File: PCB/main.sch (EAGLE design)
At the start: 52 parts, among them X1 BU-SMA-V

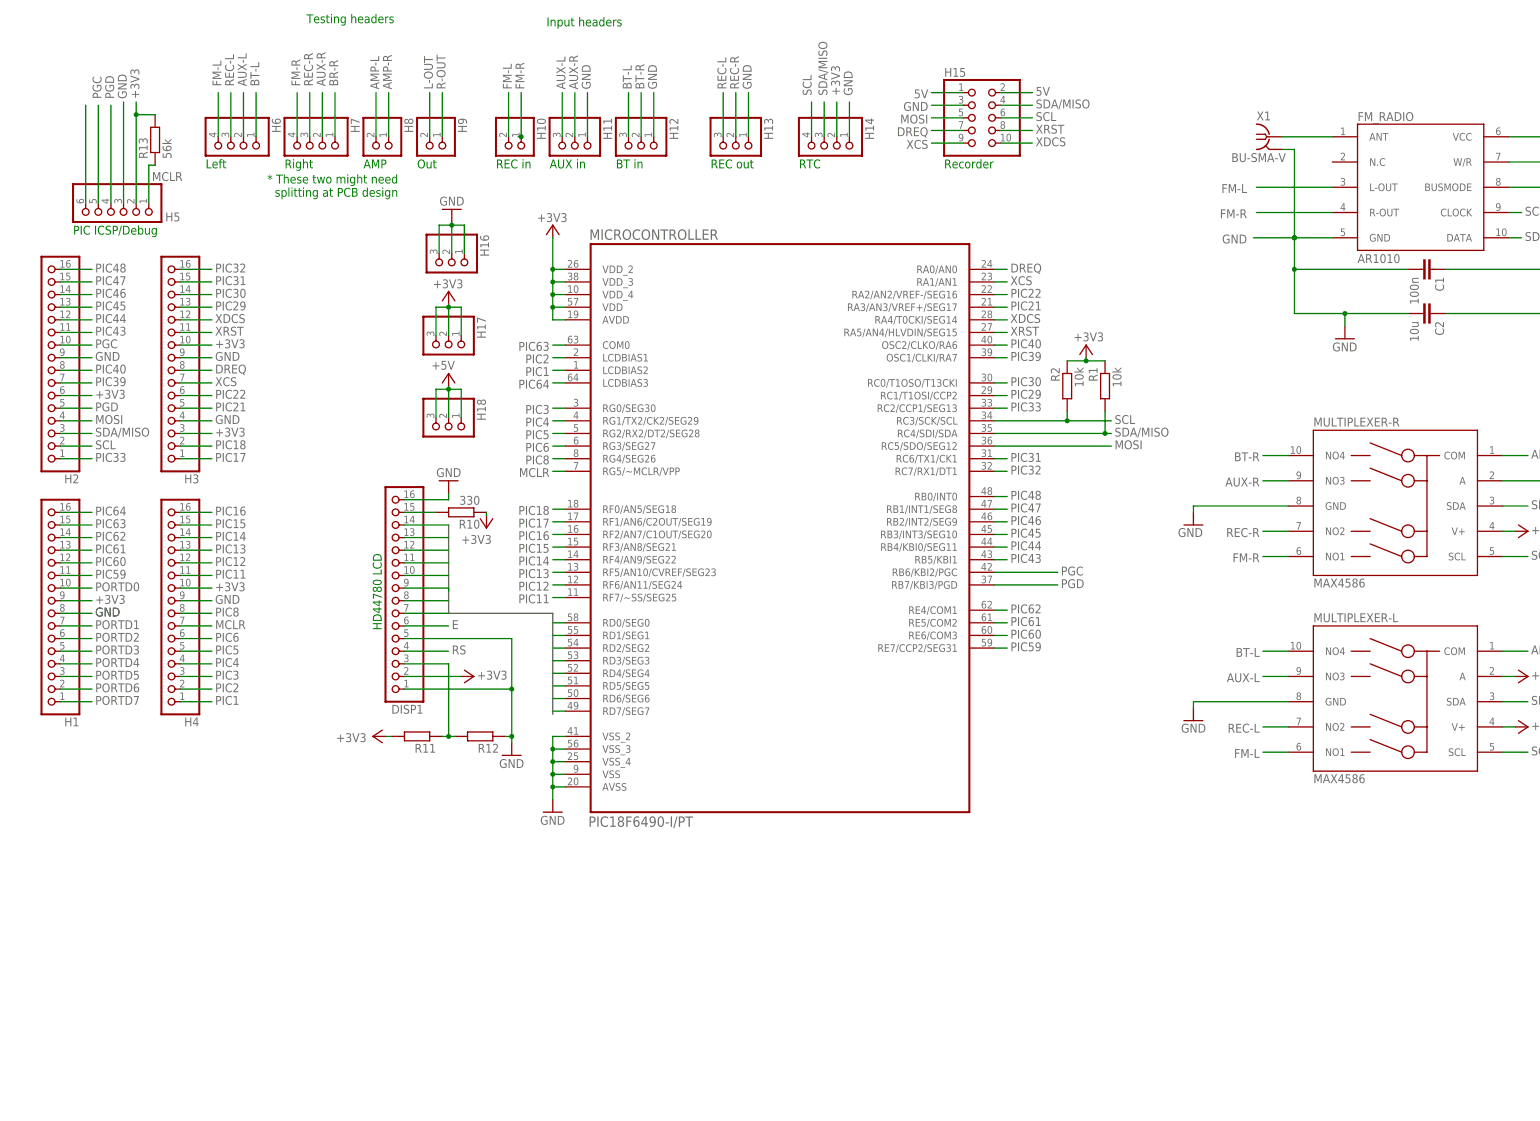
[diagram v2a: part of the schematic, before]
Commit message: Eagle Schematic Changes
Added level shifters
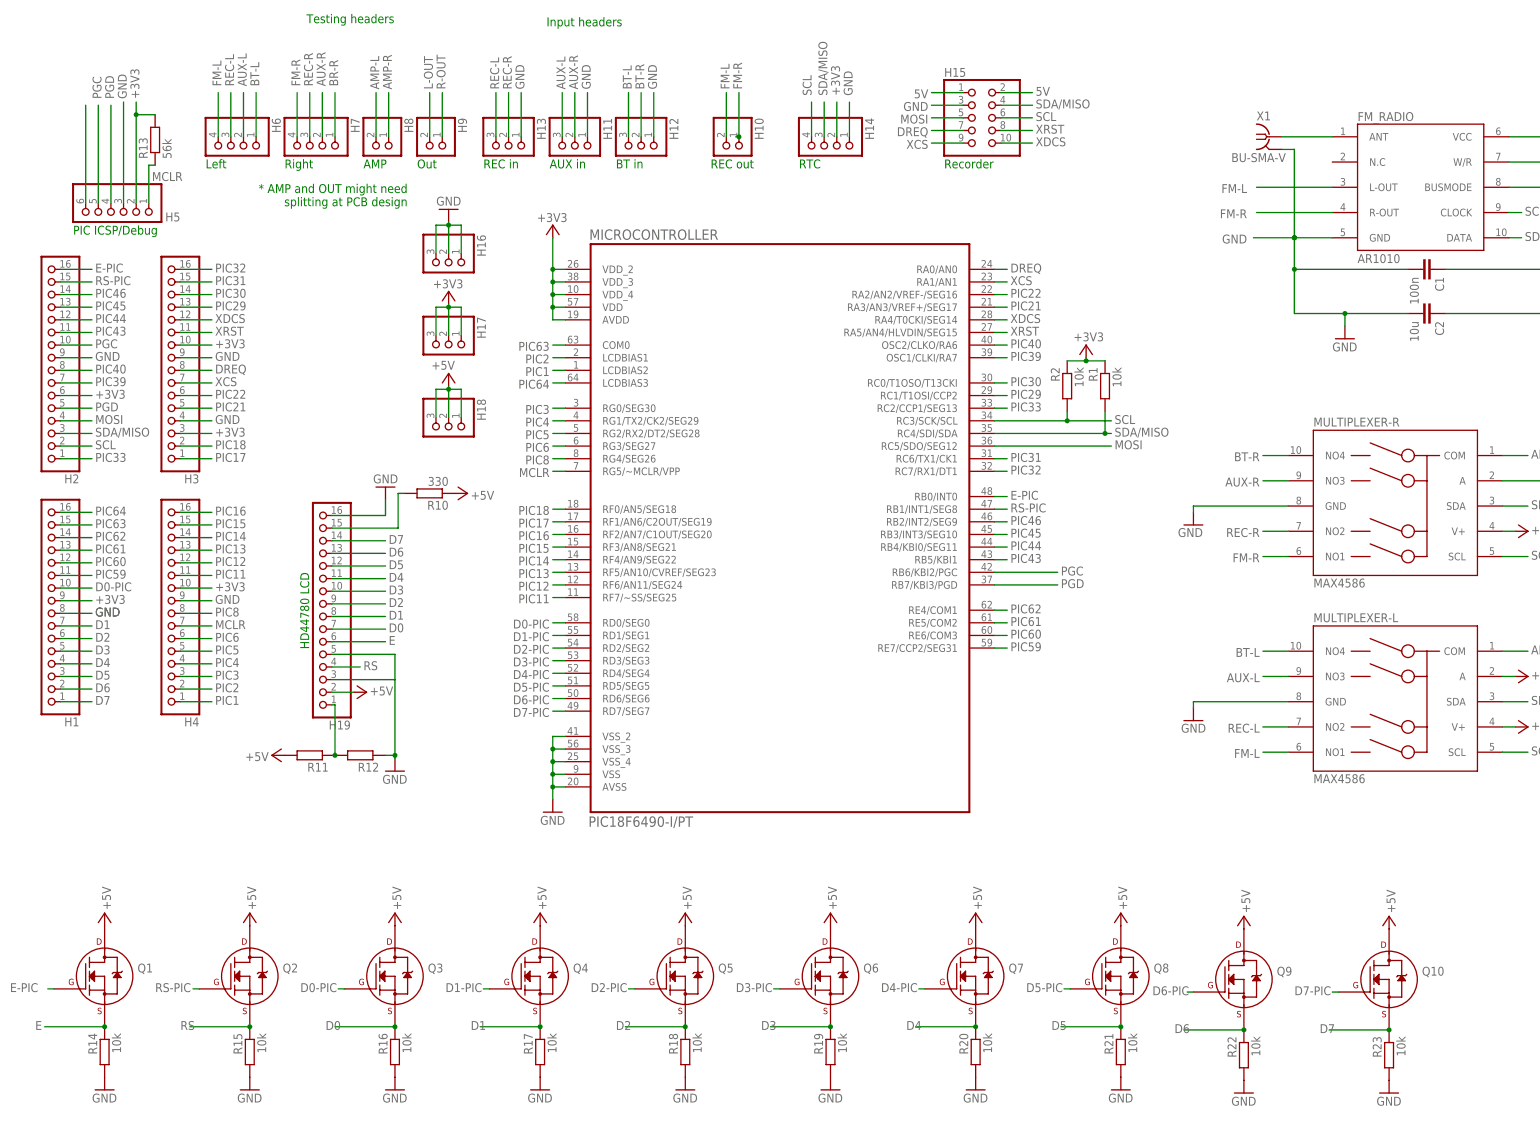
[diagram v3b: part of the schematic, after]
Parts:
- removed DISP1: (no value), pinhead:PINHD-1X16
- added H19: (no value), pinhead:PINHD-1X16
- added Q1, Q10, Q2, Q3, Q4, Q5, Q6, Q7, Q8, Q9: (no value), transistors:2N7000_SOT23
- added R14, R15, R16, R17, R18, R19, R20, R21, R22, R23: 10k, resistor:R-EU_M0805
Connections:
- removed net N$2: DISP1.15, R10.2
- removed net PIC47: H2.15, MICROCONTROLLER.RB1/INT1/SEG8
- removed net PIC48: H2.16, MICROCONTROLLER.RB0/INT0
- removed net PORTD0: DISP1.7, H1.10, MICROCONTROLLER.RD0/SEG0
- removed net PORTD1: DISP1.8, H1.7, MICROCONTROLLER.RD1/SEG1
- removed net PORTD2: DISP1.9, H1.6, MICROCONTROLLER.RD2/SEG2
- removed net PORTD3: DISP1.10, H1.5, MICROCONTROLLER.RD3/SEG3
- removed net PORTD4: DISP1.11, H1.4, MICROCONTROLLER.RD4/SEG4
- removed net PORTD5: DISP1.12, H1.3, MICROCONTROLLER.RD5/SEG5
- removed net PORTD6: DISP1.13, H1.2, MICROCONTROLLER.RD6/SEG6
- removed net PORTD7: DISP1.14, H1.1, MICROCONTROLLER.RD7/SEG7
- new net D0: H19.7, Q3.S, R16.1
- new net D0-PIC: H1.10, MICROCONTROLLER.RD0/SEG0, Q3.G
- new net D1: H1.7, H19.8, Q4.S, R17.1
- new net D1-PIC: MICROCONTROLLER.RD1/SEG1, Q4.G
- new net D2: H1.6, H19.9, Q5.S, R18.1
- new net D2-PIC: MICROCONTROLLER.RD2/SEG2, Q5.G
- new net D3: H1.5, H19.10, Q6.S, R19.1
- new net D3-PIC: MICROCONTROLLER.RD3/SEG3, Q6.G
- new net D4: H1.4, H19.11, Q7.S, R20.1
- new net D4-PIC: MICROCONTROLLER.RD4/SEG4, Q7.G
- new net D5: H1.3, H19.12, Q8.S, R21.1
- new net D5-PIC: MICROCONTROLLER.RD5/SEG5, Q8.G
- new net D6: H1.2, H19.13, Q9.S, R22.1
- new net D6-PIC: MICROCONTROLLER.RD6/SEG6, Q9.G
- new net D7: H1.1, H19.14, Q10.S, R23.1
- new net D7-PIC: MICROCONTROLLER.RD7/SEG7, Q10.G
- new net E-PIC: H2.16, MICROCONTROLLER.RB0/INT0, Q1.G
- new net N$20: H19.15, R10.2
- new net RS-PIC: H2.15, MICROCONTROLLER.RB1/INT1/SEG8, Q2.G
- net +3V3: no longer DISP1.2, R10.1, R11.2
- net +5V: now also H19.2, Q1.D, Q10.D, Q2.D, Q3.D, Q4.D, Q5.D, Q6.D, Q7.D, Q8.D, Q9.D, R10.1, R11.2
- net E: now also H19.6, Q1.S, R14.1; no longer DISP1.6
- net GND: now also H19.16, H19.3, H19.5, R14.2, R15.2, R16.2, R17.2, R18.2, R19.2, R20.2, R21.2, R22.2, R23.2; no longer DISP1.1, DISP1.16, DISP1.5
- net N$13: now also H19.1; no longer DISP1.3
- net RS: now also H19.4, Q2.S, R15.1; no longer DISP1.4
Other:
- note added: "* AMP and OUT might need splitting at PCB design"
- note removed: "* These two might need splitting at PCB design"
- moved on the sheet: H10, H13, H16, R10, R11, R12

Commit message: Initial PCB layout
~75% complete.
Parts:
- removed C6, C9: 470u, rcl:C-EUC0805
- removed R9: 4.7, resistor:R-EU_M0805
- added +5V: LSP11, solpad:LSP11
- added C13, C14, C15, C16, C17, C18: 100n, rcl:C-EUC0805
- added C20, C21: 100u, cap-pan40:C-PR-SMD-SV-D
- added R24, R25, R26: 10, resistor:R-EU_M0805
- C5, C8: value 100u -> 470u; device rcl:C-EUC0805 -> cap-pan40:C-PR-SMD-SV-G
- H6, H7: device pinhead:PINHD-1X4/90 -> pinhead:PINHD-1X4
- R6: value 4.7 -> 10
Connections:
- removed net N$12: AMP-R.-IN, C5.1
- removed net N$16: C10.2, R9.2
- new net N$1: AMP-R.-IN, C20.+
- new net N$10: C10.2, R25.2, R26.2
- new net N$2: +5V.MP, C4.1, VOLTAGE_REGULATOR.VIN
- net +3V3: now also C13.2, C14.2, C15.2, C16.2, C17.2, C18.2
- net +5V: no longer C4.1, VOLTAGE_REGULATOR.VIN
- net D1: no longer H1.7
- net D1-PIC: now also H1.7
- net D2: no longer H1.6
- net D2-PIC: now also H1.6
- net D3: no longer H1.5
- net D3-PIC: now also H1.5
- net D4: no longer H1.4
- net D4-PIC: now also H1.4
- net D5: no longer H1.3
- net D5-PIC: now also H1.3
- net D6: no longer H1.2
- net D6-PIC: now also H1.2
- net D7: no longer H1.1
- net D7-PIC: now also H1.1
- net GND: now also C13.1, C14.1, C15.1, C16.1, C17.1, C18.1, C20.-, C21.-, R24.1, R25.1, R26.1; no longer C5.2, C8.2, R9.1
- net L-OUT: now also C5.+; no longer C9.1
- net N$14: now also C21.+; no longer C8.1
- net N$5: now also C5.-; no longer C9.2
- net N$61: now also R24.2
- net N$7: now also C8.-; no longer C6.2
- net R-OUT: now also C8.+; no longer C6.1
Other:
- moved on the sheet: H16, H17, H18, R6

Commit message: PCB Schematic Change
5V Supply Pad was not connected to 5V net
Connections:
- removed net N$2: +5V.MP, C4.1, VOLTAGE_REGULATOR.VIN
- net +5V: now also +5V.MP, C4.1, VOLTAGE_REGULATOR.VIN
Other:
- moved on the sheet: C13, C14, C17, C18, C20, C21, H10, H11, H12, H13, H14, H5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

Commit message: PCB Layout
- Reworked the whole board to shrink it significantly
- Added DRC check file
- Fixed BT audio net name
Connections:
- removed net BR-R: H7.1
- removed net PIC61: H1.13, MICROCONTROLLER.RE5/COM2
- removed net PIC62: H1.14, MICROCONTROLLER.RE4/COM1
- new net PIC47: H2.15, MICROCONTROLLER.RB1/INT1/SEG8
- new net PIC48: H2.16, MICROCONTROLLER.RB0/INT0
- net BT-R: now also H7.1
- net E-PIC: now also H1.13; no longer H2.16, MICROCONTROLLER.RB0/INT0
- net RS-PIC: now also H1.14, MICROCONTROLLER.RE4/COM1; no longer H2.15, MICROCONTROLLER.RB1/INT1/SEG8
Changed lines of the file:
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@@
 <setting verticaltext="up"/>
 </settings>
-<grid distance="0.025" unitdist="inch" unit="inch" style="lines" multiple="1" display="yes" altdistance="0.01" altunitdist="inch" altunit="inch"/>
+<grid distance="0.025" unitdist="inch" unit="inch" style="lines" multiple="1" display="no" altdistance="0.01" altunitdist="inch" altunit="inch"/>
 <layers>
 <layer number="1" name="Top" color="4" fill="1" visible="no" active="no"/>
@@
 <pinref part="C4" gate="G$1" pin="2"/>
 <wire x1="255.905" y1="93.345" x2="255.905" y2="94.615" width="0.1524" layer="91"/>
-<pinref part="0V" gate="1" pin="MP"/>
 <pinref part="VOLTAGE_REGULATOR" gate="A" pin="GND"/>
 <wire x1="263.525" y1="99.695" x2="266.065" y2="99.695" width="0.1524" layer="91"/>
 <wire x1="263.525" y1="99.695" x2="263.525" y2="94.615" width="0.1524" layer="91"/>
-<wire x1="246.38" y1="94.615" x2="255.905" y2="94.615" width="0.1524" layer="91"/>
 <wire x1="255.905" y1="94.615" x2="263.525" y2="94.615" width="0.1524" layer="91"/>
 <wire x1="255.905" y1="96.52" x2="255.905" y2="94.615" width="0.1524" layer="91"/>
 <junction x="255.905" y="94.615"/>
+<pinref part="0V" gate="1" pin="MP"/>
+<wire x1="246.38" y1="94.615" x2="255.905" y2="94.615" width="0.1524" layer="91"/>
 </segment>
 <segment>
@@
 </segment>
 </net>
-<net name="PIC62" class="0">
-<segment>
-<pinref part="H1" gate="A" pin="14"/>
-<wire x1="-85.725" y1="52.705" x2="-79.375" y2="52.705" width="0.1524" layer="91"/>
-<label x="-78.74" y="52.07" size="1.778" layer="95"/>
-</segment>
-<segment>
-<pinref part="MICROCONTROLLER" gate="A" pin="RE4/COM1"/>
-<wire x1="102.235" y1="38.1" x2="104.775" y2="38.1" width="0.1524" layer="91"/>
-<label x="105.41" y="37.465" size="1.778" layer="95"/>
-</segment>
-</net>
-<net name="PIC61" class="0">
-<segment>
-<pinref part="H1" gate="A" pin="13"/>
-<wire x1="-85.725" y1="50.165" x2="-79.375" y2="50.165" width="0.1524" layer="91"/>
-<label x="-78.74" y="49.53" size="1.778" layer="95"/>
-</segment>
-<segment>
-<pinref part="MICROCONTROLLER" gate="A" pin="RE5/COM2"/>
-<wire x1="102.235" y1="35.56" x2="104.775" y2="35.56" width="0.1524" layer="91"/>
-<label x="105.41" y="34.925" size="1.778" layer="95"/>
-</segment>
-</net>
 <net name="PIC60" class="0">
 <segment>
@@
 <label x="155.575" y="69.85" size="1.778" layer="95" rot="R180"/>
 </segment>
-</net>
-<net name="BR-R" class="0">
 <segment>
 <pinref part="H7" gate="A" pin="1"/>
@@
 <net name="E-PIC" class="0">
 <segment>
-<pinref part="MICROCONTROLLER" gate="A" pin="RB0/INT0"/>
-<wire x1="102.235" y1="60.96" x2="104.775" y2="60.96" width="0.1524" layer="91"/>
-<label x="105.41" y="60.325" size="1.778" layer="95"/>
-</segment>
-<segment>
-<pinref part="H2" gate="A" pin="16"/>
-<wire x1="-85.725" y1="106.68" x2="-79.375" y2="106.68" width="0.1524" layer="91"/>
-<label x="-78.74" y="106.045" size="1.778" layer="95"/>
-</segment>
-<segment>
 <pinref part="Q1" gate="G$1" pin="G"/>
 <wire x1="-86.995" y1="-38.1" x2="-88.265" y2="-38.1" width="0.1524" layer="91"/>
 <label x="-95.885" y="-38.735" size="1.778" layer="95"/>
 </segment>
+<segment>
+<pinref part="H1" gate="A" pin="13"/>
+<wire x1="-85.725" y1="50.165" x2="-79.375" y2="50.165" width="0.1524" layer="91"/>
+<label x="-78.74" y="49.53" size="1.778" layer="95"/>
+</segment>
+<segment>
+<wire x1="102.235" y1="35.56" x2="104.775" y2="35.56" width="0.1524" layer="91"/>
+<label x="105.41" y="34.925" size="1.778" layer="95"/>
+</segment>
 </net>
 <net name="RS-PIC" class="0">
-<segment>
-<pinref part="MICROCONTROLLER" gate="A" pin="RB1/INT1/SEG8"/>
-<wire x1="102.235" y1="58.42" x2="104.775" y2="58.42" width="0.1524" layer="91"/>
-<label x="105.41" y="57.785" size="1.778" layer="95"/>
-</segment>
-<segment>
-<pinref part="H2" gate="A" pin="15"/>
-<wire x1="-85.725" y1="104.14" x2="-79.375" y2="104.14" width="0.1524" layer="91"/>
-<label x="-78.74" y="103.505" size="1.778" layer="95"/>
-</segment>
 <segment>
 <pinref part="Q2" gate="G$1" pin="G"/>
 <wire x1="-57.785" y1="-38.1" x2="-59.055" y2="-38.1" width="0.1524" layer="91"/>
 <label x="-66.675" y="-38.735" size="1.778" layer="95"/>
+</segment>
+<segment>
+<pinref part="MICROCONTROLLER" gate="A" pin="RE4/COM1"/>
+<wire x1="102.235" y1="38.1" x2="104.775" y2="38.1" width="0.1524" layer="91"/>
+<label x="105.41" y="37.465" size="1.778" layer="95"/>
+</segment>
+<segment>
+<pinref part="H1" gate="A" pin="14"/>
+<wire x1="-85.725" y1="52.705" x2="-79.375" y2="52.705" width="0.1524" layer="91"/>
+<label x="-78.74" y="52.07" size="1.778" layer="95"/>
 </segment>
 </net>
@@
 </segment>
 </net>
+<net name="PIC47" class="0">
+<segment>
+<pinref part="MICROCONTROLLER" gate="A" pin="RB1/INT1/SEG8"/>
+<wire x1="102.235" y1="58.42" x2="104.775" y2="58.42" width="0.1524" layer="91"/>
+<label x="105.41" y="57.785" size="1.778" layer="95"/>
+</segment>
+<segment>
+<pinref part="H2" gate="A" pin="15"/>
+<wire x1="-85.725" y1="104.14" x2="-79.375" y2="104.14" width="0.1524" layer="91"/>
+<label x="-78.74" y="103.505" size="1.778" layer="95"/>
+</segment>
+</net>
+<net name="PIC48" class="0">
+<segment>
+<pinref part="MICROCONTROLLER" gate="A" pin="RB0/INT0"/>
+<wire x1="102.235" y1="60.96" x2="104.775" y2="60.96" width="0.1524" layer="91"/>
+<label x="105.41" y="60.325" size="1.778" layer="95"/>
+</segment>
+<segment>
+<pinref part="H2" gate="A" pin="16"/>
+<wire x1="-85.725" y1="106.68" x2="-79.375" y2="106.68" width="0.1524" layer="91"/>
+<label x="-78.74" y="106.045" size="1.778" layer="95"/>
+</segment>
+</net>

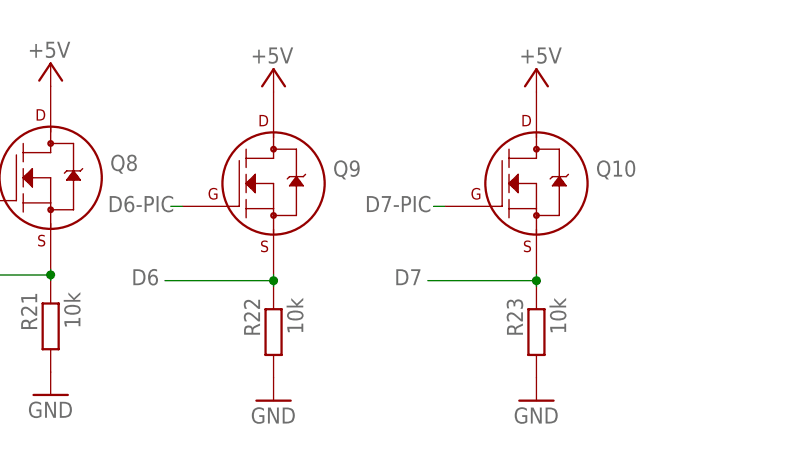
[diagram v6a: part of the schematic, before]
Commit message: PCB Layout
-Track widths fixed
-Routing through headers neatened
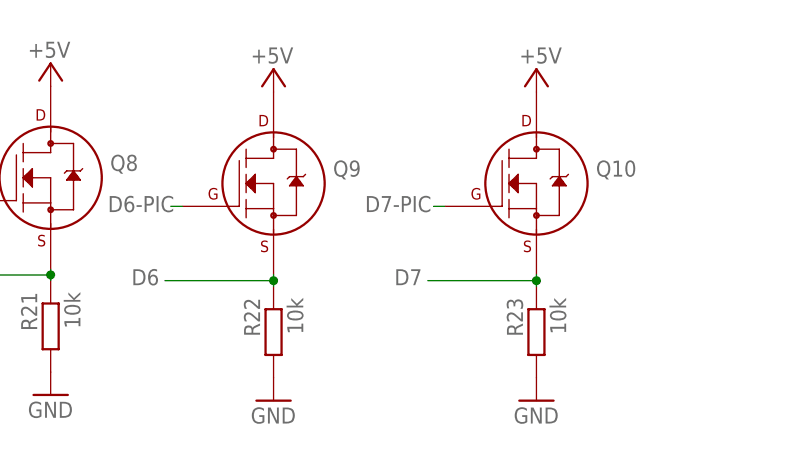
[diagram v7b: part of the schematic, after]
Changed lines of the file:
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@@
 <setting verticaltext="up"/>
 </settings>
-<grid distance="0.025" unitdist="inch" unit="inch" style="lines" multiple="1" display="no" altdistance="0.01" altunitdist="inch" altunit="inch"/>
+<grid distance="0.1" unitdist="inch" unit="inch" style="lines" multiple="1" display="no" altdistance="0.01" altunitdist="inch" altunit="inch"/>
 <layers>
 <layer number="1" name="Top" color="4" fill="1" visible="no" active="no"/>
@@
 <segment>
 <pinref part="Q10" gate="G$1" pin="S"/>
-<wire x1="181.61" y1="-47.625" x2="181.61" y2="-46.99" width="0.1524" layer="91"/>
 <wire x1="181.61" y1="-46.99" x2="169.545" y2="-46.99" width="0.1524" layer="91"/>
 <pinref part="R23" gate="G$1" pin="1"/>
@@
 <segment>
 <pinref part="Q9" gate="G$1" pin="S"/>
-<wire x1="152.4" y1="-47.625" x2="152.4" y2="-46.99" width="0.1524" layer="91"/>
 <wire x1="152.4" y1="-46.99" x2="140.335" y2="-46.99" width="0.1524" layer="91"/>
 <pinref part="R22" gate="G$1" pin="1"/>

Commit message: PCB + Schematic
- E-Pic issue fixed
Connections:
- net E-PIC: now also MICROCONTROLLER.RE5/COM2
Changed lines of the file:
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@@
 <setting verticaltext="up"/>
 </settings>
-<grid distance="0.1" unitdist="inch" unit="inch" style="lines" multiple="1" display="no" altdistance="0.01" altunitdist="inch" altunit="inch"/>
+<grid distance="0.025" unitdist="inch" unit="inch" style="lines" multiple="1" display="yes" altdistance="0.01" altunitdist="inch" altunit="inch"/>
 <layers>
 <layer number="1" name="Top" color="4" fill="1" visible="no" active="no"/>
@@
 </segment>
 <segment>
+<pinref part="MICROCONTROLLER" gate="A" pin="RE5/COM2"/>
 <wire x1="102.235" y1="35.56" x2="104.775" y2="35.56" width="0.1524" layer="91"/>
 <label x="105.41" y="34.925" size="1.778" layer="95"/>
